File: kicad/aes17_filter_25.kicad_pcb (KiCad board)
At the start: 2 copper layers, 179.8 x 90 mm, 35 parts, among them J1 NC3FAAH, J2 NC3MAAH, J3 Conn_01x01_Pin, J4 Conn_01x01_Pin, SW2 SW_DPDT_x2

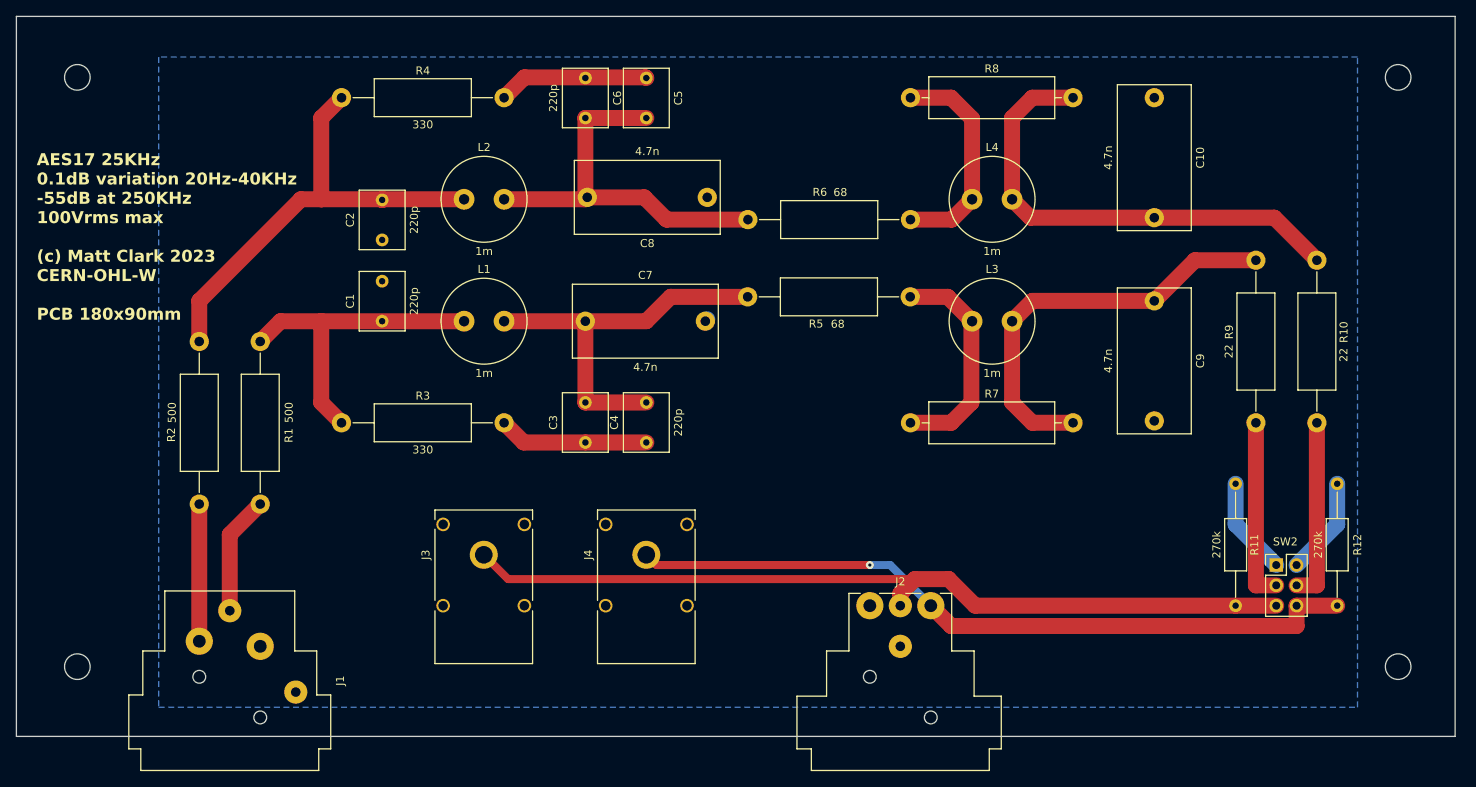
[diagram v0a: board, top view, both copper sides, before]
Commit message: Updated based on ASR commentary.  See README for details
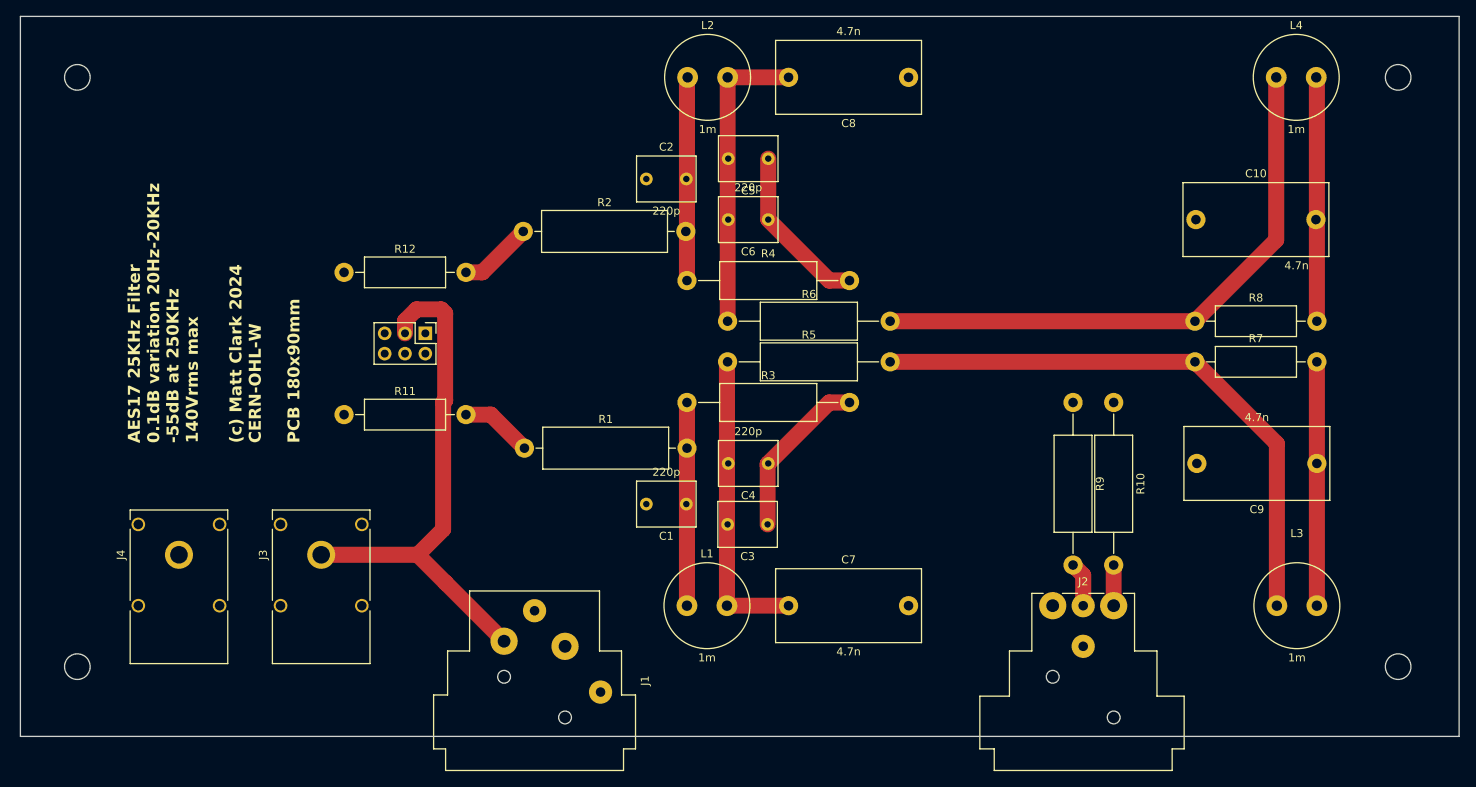
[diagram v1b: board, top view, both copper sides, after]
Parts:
- removed SW2: SW_DPDT_x2, Connector_PinHeader_2.54mm:PinHeader_2x03_P2.54mm_Vertical
- added SW1: SW_DPDT_x2, Connector_PinHeader_2.54mm:PinHeader_2x03_P2.54mm_Vertical, F.Cu at (101.9, 87.9)
- R1, R2: footprint Resistor_THT:R_Axial_DIN0414_L11.9mm_D4.5mm_P20.32mm_Horizontal -> Resistor_THT:R_Axial_DIN0516_L15.5mm_D5.0mm_P20.32mm_Horizontal
- R11, R12: value 270k -> 4k5; footprint Resistor_THT:R_Axial_DIN0207_L6.3mm_D2.5mm_P15.24mm_Horizontal -> Resistor_THT:R_Axial_DIN0411_L9.9mm_D3.6mm_P15.24mm_Horizontal
- R7, R8: footprint Resistor_THT:R_Axial_DIN0516_L15.5mm_D5.0mm_P20.32mm_Horizontal -> Resistor_THT:R_Axial_DIN0411_L9.9mm_D3.6mm_P15.24mm_Horizontal
- moved R12 126.9 mm to (91.8, 80.3), turned to 0 degrees
- moved R11 111.8 mm to (91.8, 98.0), turned to 0 degrees
- moved J4 58.4 mm to (71.1, 115.6)
- moved R2 52.9 mm to (114.2, 75.1), turned to 0 degrees
- moved L3 52.1 mm to (208.4, 121.9)
- moved R4 48.9 mm to (134.6, 81.3)
- moved R8 45.2 mm to (198.1, 86.4)
- moved L1 45.2 mm to (134.6, 121.9)
- moved C1 44.4 mm to (134.5, 109.2), turned to 180 degrees
- moved C7 43.7 mm to (147.3, 121.9)
- moved R3 43.3 mm to (134.6, 96.5)
- moved L4 41.0 mm to (208.3, 55.9)
- moved J1 38.1 mm to (119.4, 127.0)
- moved R7 36.4 mm to (198.1, 91.4)
- moved C2 33.9 mm to (129.5, 68.6), turned to 0 degrees
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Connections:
- J1 pad 2: Net-(J1-Pad2) -> Net-(J3-Pin_1)
- J1 pad 3: Net-(J1-Pad3) -> Net-(J4-Pin_1)
- J2 pad 2: Net-(J4-Pin_1) -> Net-(J2-Pad2)
- J2 pad 3: Net-(J3-Pin_1) -> Net-(J2-Pad3)
- R1 pad 1: Net-(J1-Pad3) -> Net-(SW1B-A)
- R10 pad 2: Net-(SW2B-B) -> Net-(J2-Pad2)
- R11 pad 2: Net-(J3-Pin_1) -> Net-(SW1B-A)
- R12 pad 2: Net-(J4-Pin_1) -> Net-(SW1A-A)
- R2 pad 1: Net-(J1-Pad2) -> Net-(SW1A-A)
- R9 pad 2: Net-(SW2A-B) -> Net-(J2-Pad3)
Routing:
- net Net-(L4-Pad1): track 27.6 -> 72.8 mm
- net Net-(L3-Pad1): track 27.9 -> 72.8 mm
- net Net-(J3-Pin_1): track 105.8 -> 66.3 mm
- net Net-(C2-Pad2): track 57.3 -> 25.4 mm
- net Net-(SW2B-B): track 22.9 -> 0.00 mm
- net Net-(SW2A-B): track 22.9 -> 0.00 mm
- net Net-(SW1A-A): track 0.00 -> 19.4 mm
- net Net-(SW1B-A): track 0.00 -> 18.8 mm
- net Net-(J4-Pin_1): track 92.6 -> 74.8 mm, vias 1 -> 0
- net Net-(J1-Pad2): track 17.1 -> 0.00 mm
- net Net-(J1-Pad3): track 14.9 -> 0.00 mm
- net Net-(C1-Pad1): track 40.3 -> 25.4 mm
- net Net-(C9-Pad1): track 52.5 -> 65.3 mm
- net Net-(C3-Pad2): track 49.5 -> 38.2 mm
- net Net-(C5-Pad2): track 49.4 -> 38.1 mm
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- added copper zone on In1.Cu, net GND
- removed copper zone on B.Cu, net GND
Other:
- copper layers 2 -> 4
- board text added: "(c) Matt Clark 2024 CERN-OHL-W PCB 180x90mm"
- board text added: "AES17 25KHz Filter 0.1dB variation 20Hz-20KHz -55dB at 250KHz 140Vrms max"
- board text removed: "AES17 25KHz 0.1dB variation 20Hz-40KHz -55dB at 250KHz 100Vrms max (c) Matt Clark 2023 CERN-OHL-W PCB 180x90mm"

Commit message: spaced inductors out more, added ground jack
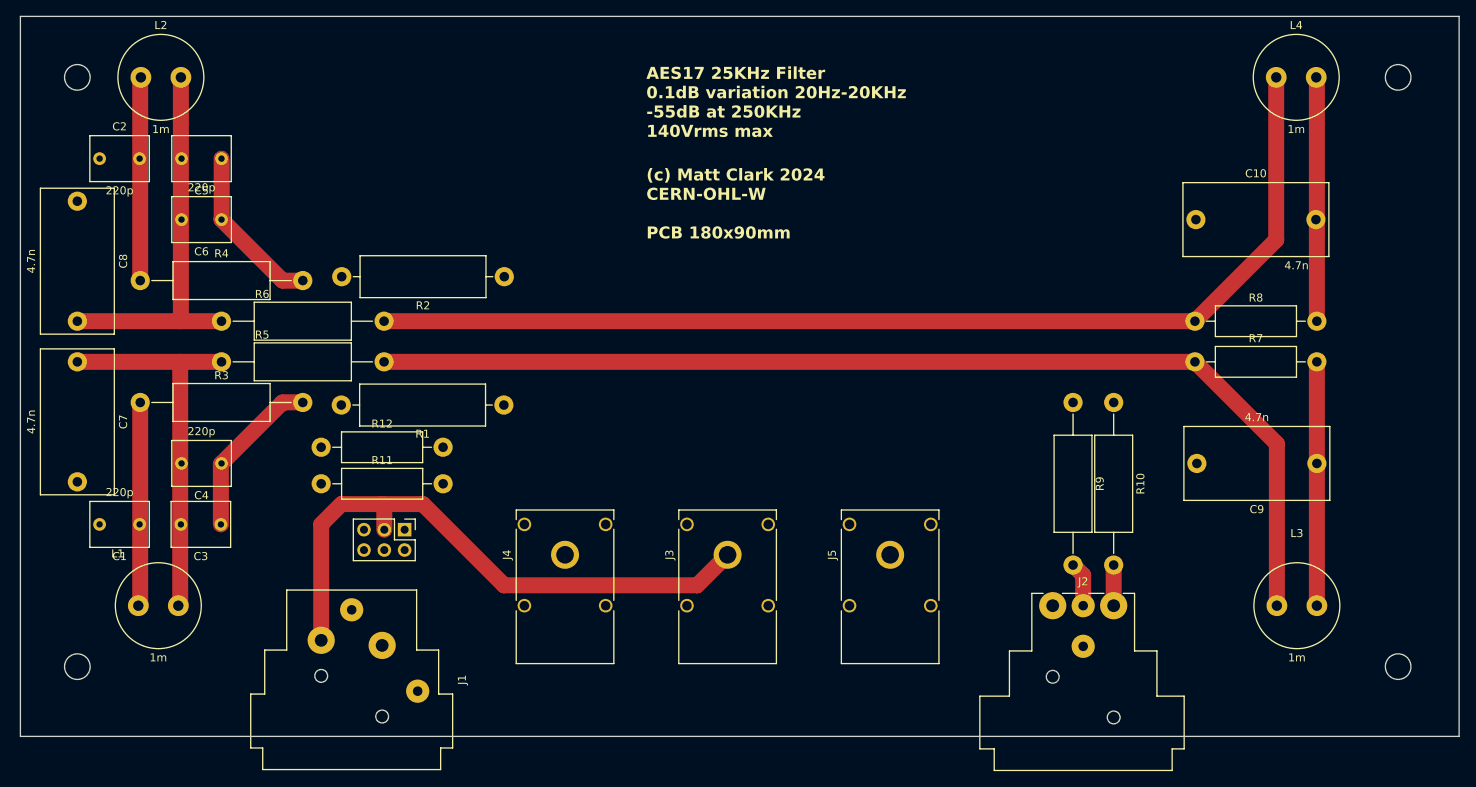
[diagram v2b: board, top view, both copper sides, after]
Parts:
- added J5: Conn_01x01_Pin, Connector:Banana_Cliff_FCR7350L_S16N-PC_Horizontal, F.Cu at (160.0, 115.6)
- J3: footprint Connector:Banana_Cliff_FCR7350x_S16N-PC_Horizontal -> Connector:Banana_Cliff_FCR7350R_S16N-PC_Horizontal
- J4: footprint Connector:Banana_Cliff_FCR7350x_S16N-PC_Horizontal -> Connector:Banana_Cliff_FCR7350B_S16N-PC_Horizontal
- moved C8 105.0 mm to (58.4, 71.4), turned to -90 degrees
- moved C7 94.0 mm to (58.4, 91.4), turned to -90 degrees
- moved L1 68.6 mm to (66.0, 121.9)
- moved C1 68.4 mm to (66.2, 111.8)
- moved C2 68.4 mm to (61.2, 66.0)
- moved C4 68.3 mm to (76.4, 104.1)
- moved C5 68.3 mm to (76.4, 66.0)
- moved C6 68.3 mm to (76.4, 73.7)
- moved R3 68.3 mm to (66.3, 96.5)
- moved R4 68.3 mm to (66.3, 81.3)
- moved C3 68.3 mm to (76.4, 111.8)
- moved L2 68.3 mm to (66.4, 55.9)
- moved R5 63.3 mm to (76.4, 91.4)
- moved R6 63.3 mm to (76.4, 86.4)
- moved J3 50.8 mm to (139.7, 115.6)
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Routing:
- net Net-(L4-Pad1): track 72.8 -> 136.0 mm
- net Net-(L3-Pad1): track 72.8 -> 136.1 mm
- net Net-(J4-Pin_1): track 74.8 -> 32.9 mm
- net Net-(C2-Pad2): track 25.4 -> 54.8 mm
- net Net-(C1-Pad1): track 25.4 -> 54.8 mm
- net Net-(SW1A-A): track 19.4 -> 36.3 mm
- net Net-(C5-Pad2): track 38.1 -> 48.5 mm
- net Net-(C3-Pad2): track 38.2 -> 48.5 mm
- net Net-(J3-Pin_1): track 66.3 -> 75.4 mm
- net Net-(SW1B-A): track 18.8 -> 26.0 mm
- net Net-(SW1A-C): track 9.72 -> 12.5 mm
- net Net-(SW1B-C): track 9.72 -> 11.8 mm

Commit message: Fixed minor errors, added 3d models
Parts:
- moved R9 5.08 mm to (188.0, 96.5)
- moved J2 5.08 mm to (185.4, 121.9)
- moved R10 5.08 mm to (193.0, 96.5)
- moved J3 1.18 mm to (140.9, 115.6)
- moved J4 1.18 mm to (120.6, 115.6)
- moved J5 1.18 mm to (161.2, 115.6)
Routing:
- net Net-(C10-Pad2): track 60.1 -> 55.0 mm
- net Net-(C9-Pad1): track 65.3 -> 60.7 mm
- net Net-(J3-Pin_1): track 75.4 -> 76.6 mm
- net Net-(J4-Pin_1): track 32.9 -> 34.1 mm

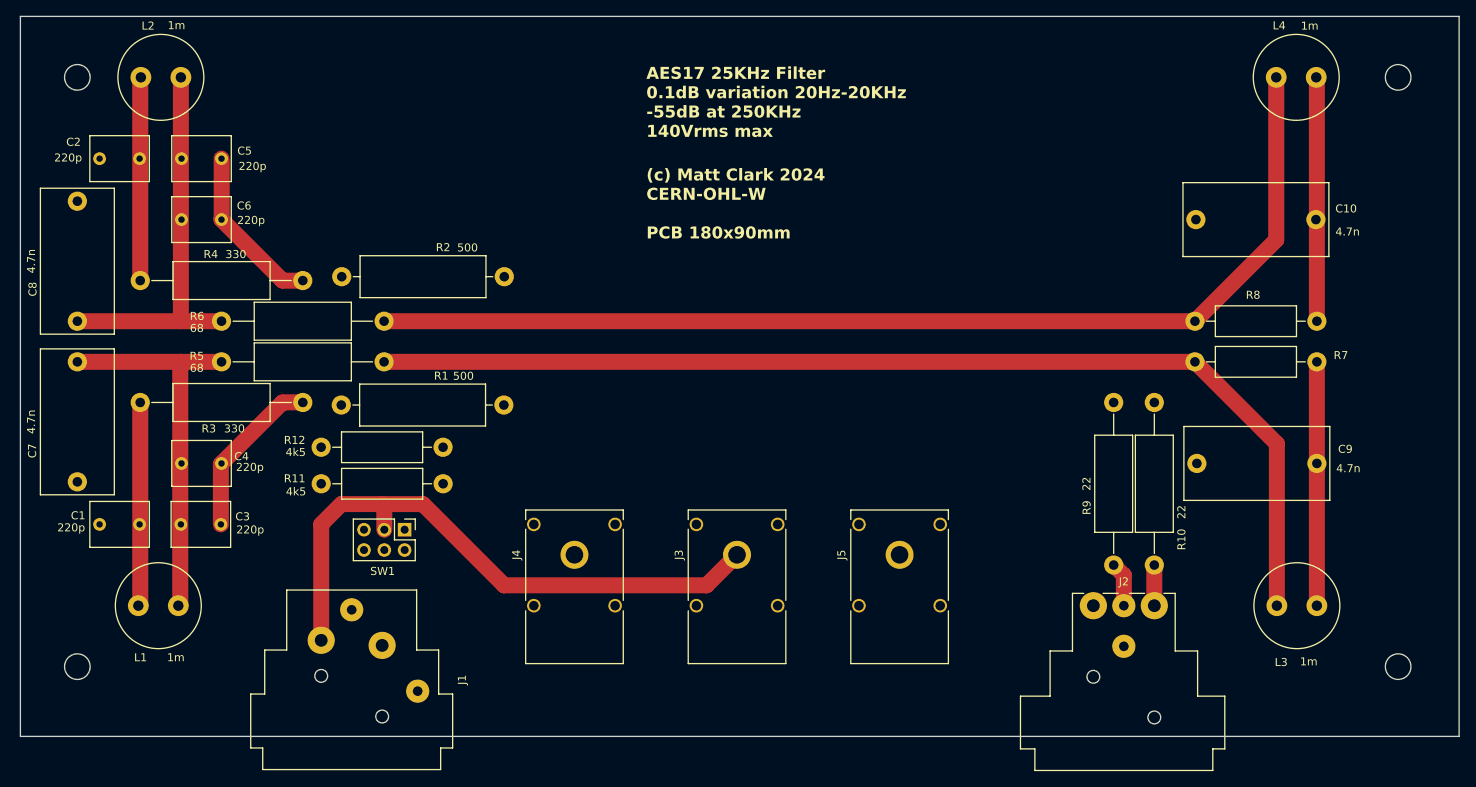
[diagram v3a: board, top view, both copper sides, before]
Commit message: reduce baord width by 5mm, add recommended hammond case to readme, move mounting holes to be 5mm inboard, change spec text on board silkscreen
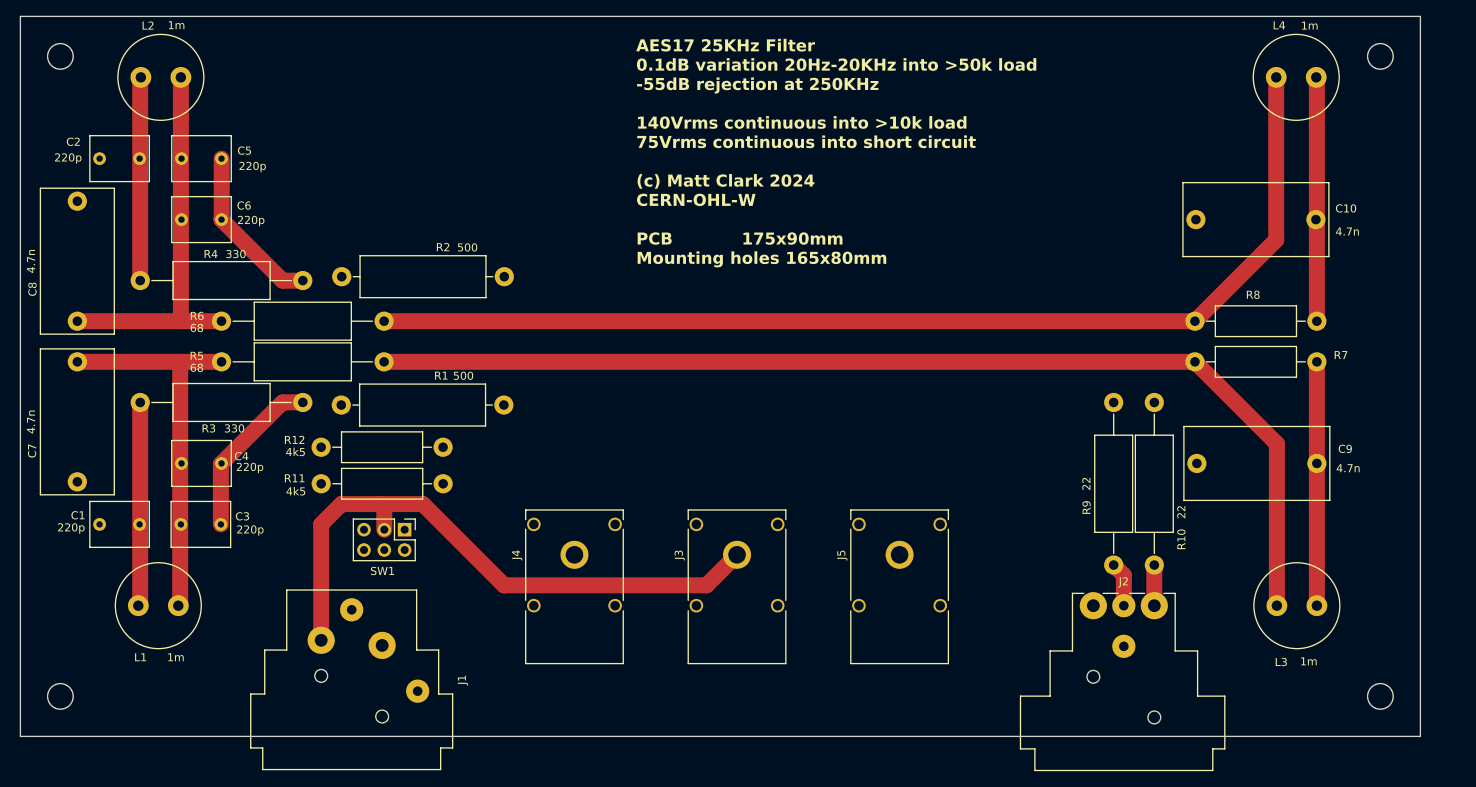
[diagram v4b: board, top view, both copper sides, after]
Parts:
- moved H4 4.33 mm to (221.3, 133.3)
- moved H3 4.28 mm to (56.3, 133.3)
- moved H2 3.43 mm to (221.3, 53.3)
- moved H1 3.37 mm to (56.3, 53.3)
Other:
- board size 179.8 x 90 mm -> 175 x 90 mm
- board text added: "AES17 25KHz Filter 0.1dB variation 20Hz-20KHz into >50k load -55dB rejection at 250KHz 140Vrms continuous into >10k load 75Vrms continuous into short circuit (c) Matt Clark 2024 CERN-OHL-W PCB 175x90mm Mounting holes 165x80mm"
- board text removed: "(c) Matt Clark 2024 CERN-OHL-W PCB 180x90mm"
- board text removed: "AES17 25KHz Filter 0.1dB variation 20Hz-20KHz -55dB at 250KHz 140Vrms max"
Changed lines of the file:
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@@
 	(footprint "MountingHole:MountingHole_3.2mm_M3"
 		(layer "F.Cu")
-		(at 223.52 55.88)
+		(at 221.3 53.26)
 		(descr "Mounting Hole 3.2mm, no annular, M3")
 		(tags "mounting hole 3.2mm no annular m3")
@@
 	(footprint "MountingHole:MountingHole_3.2mm_M3"
 		(layer "F.Cu")
-		(at 58.42 55.88)
+		(at 56.3 53.26)
 		(descr "Mounting Hole 3.2mm, no annular, M3")
 		(tags "mounting hole 3.2mm no annular m3")
@@
 	(footprint "MountingHole:MountingHole_3.2mm_M3"
 		(layer "F.Cu")
-		(at 58.42 129.54)
+		(at 56.3 133.26)
 		(descr "Mounting Hole 3.2mm, no annular, M3")
 		(tags "mounting hole 3.2mm no annular m3")
@@
 	(footprint "MountingHole:MountingHole_3.2mm_M3"
 		(layer "F.Cu")
-		(at 223.52 129.54)
+		(at 221.3 133.26)
 		(descr "Mounting Hole 3.2mm, no annular, M3")
 		(tags "mounting hole 3.2mm no annular m3")
@@
 	(gr_rect
 		(start 51.3 48.26)
-		(end 231.14 138.26)
+		(end 226.3 138.26)
 		(stroke
 			(width 0.1)
@@
 		(layer "Edge.Cuts")
 	)
-	(gr_text "AES17 25KHz Filter\n0.1dB variation 20Hz-20KHz\n-55dB at 250KHz\n140Vrms max"
-		(at 129.54 63.5 0)
-		(layer "F.SilkS")
-		(effects
-			(font
-				(size 1.5 1.5)
-				(thickness 0.3)
-				(bold yes)
-			)
-			(justify left bottom)
-		)
-	)
-	(gr_text "(c) Matt Clark 2024\nCERN-OHL-W\n\nPCB 180x90mm"
-		(at 129.54 76.2 0)
+	(gr_text "AES17 25KHz Filter\n0.1dB variation 20Hz-20KHz into >50k load\n-55dB rejection at 250KHz\n\n140Vrms continuous into >10k load\n75Vrms continuous into short circuit\n\n(c) Matt Clark 2024\nCERN-OHL-W\n\nPCB            175x90mm\nMounting holes 165x80mm"
+		(at 128.27 79.375 0)
 		(layer "F.SilkS")
 		(effects
